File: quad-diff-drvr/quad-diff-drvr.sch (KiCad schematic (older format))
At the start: 10 parts, among them J1 Raspberry_Pi_2_3, J2 Conn_01x04, J3 Conn_01x04, J4 Conn_01x04, J5 Conn_01x04, J6 Conn_01x04

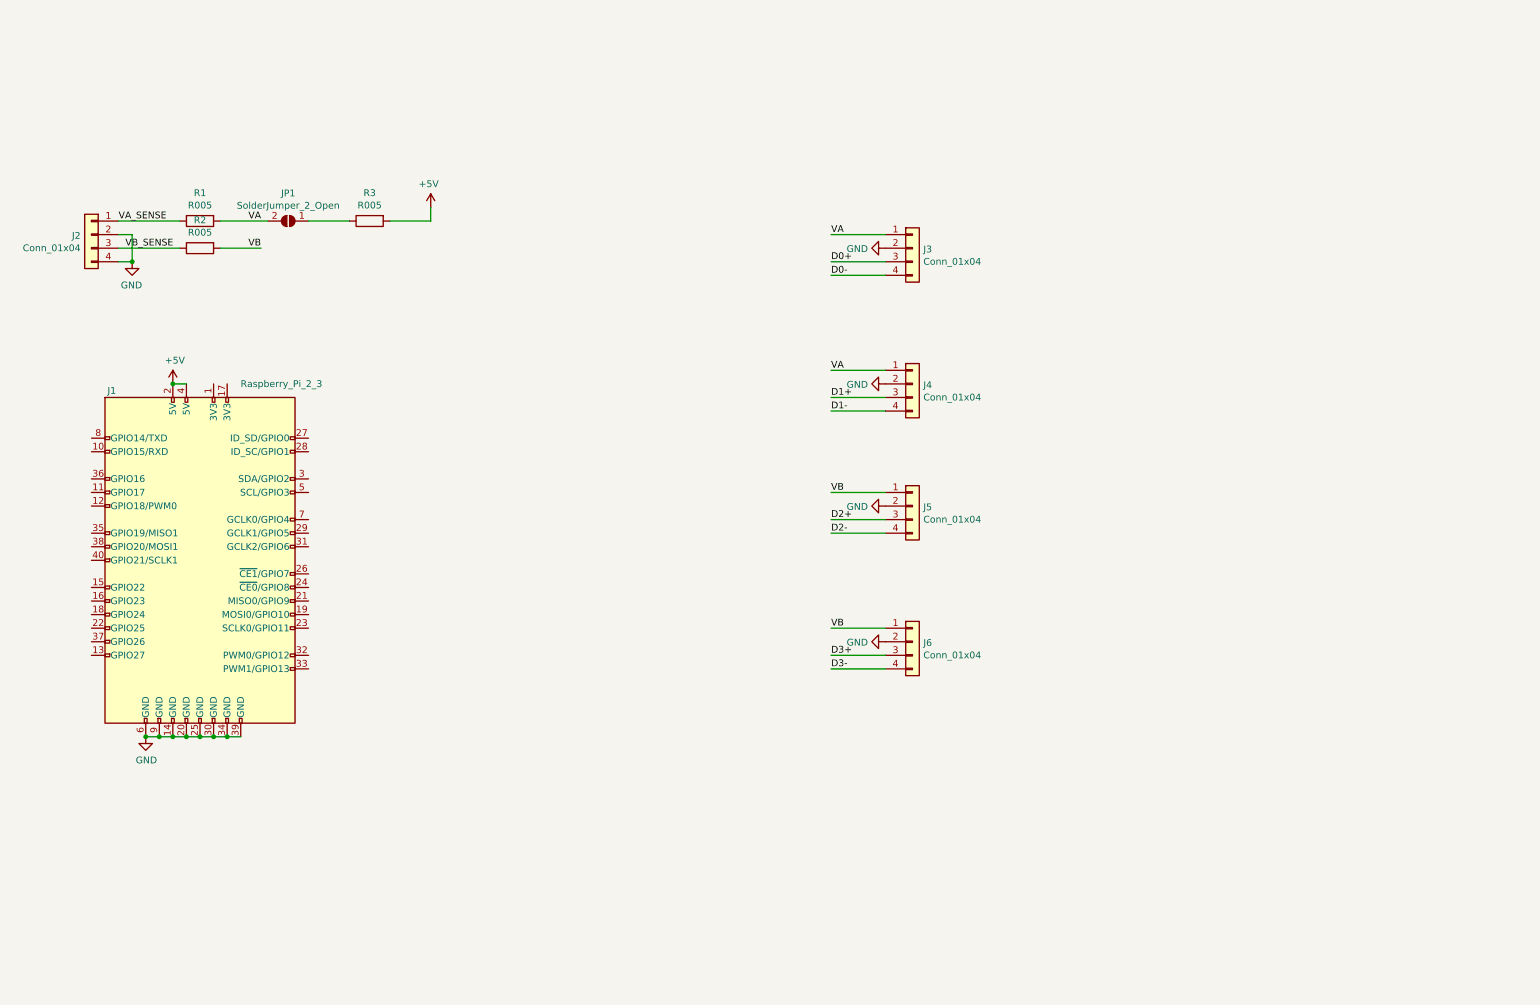
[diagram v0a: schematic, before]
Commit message: qdd: power monitor added
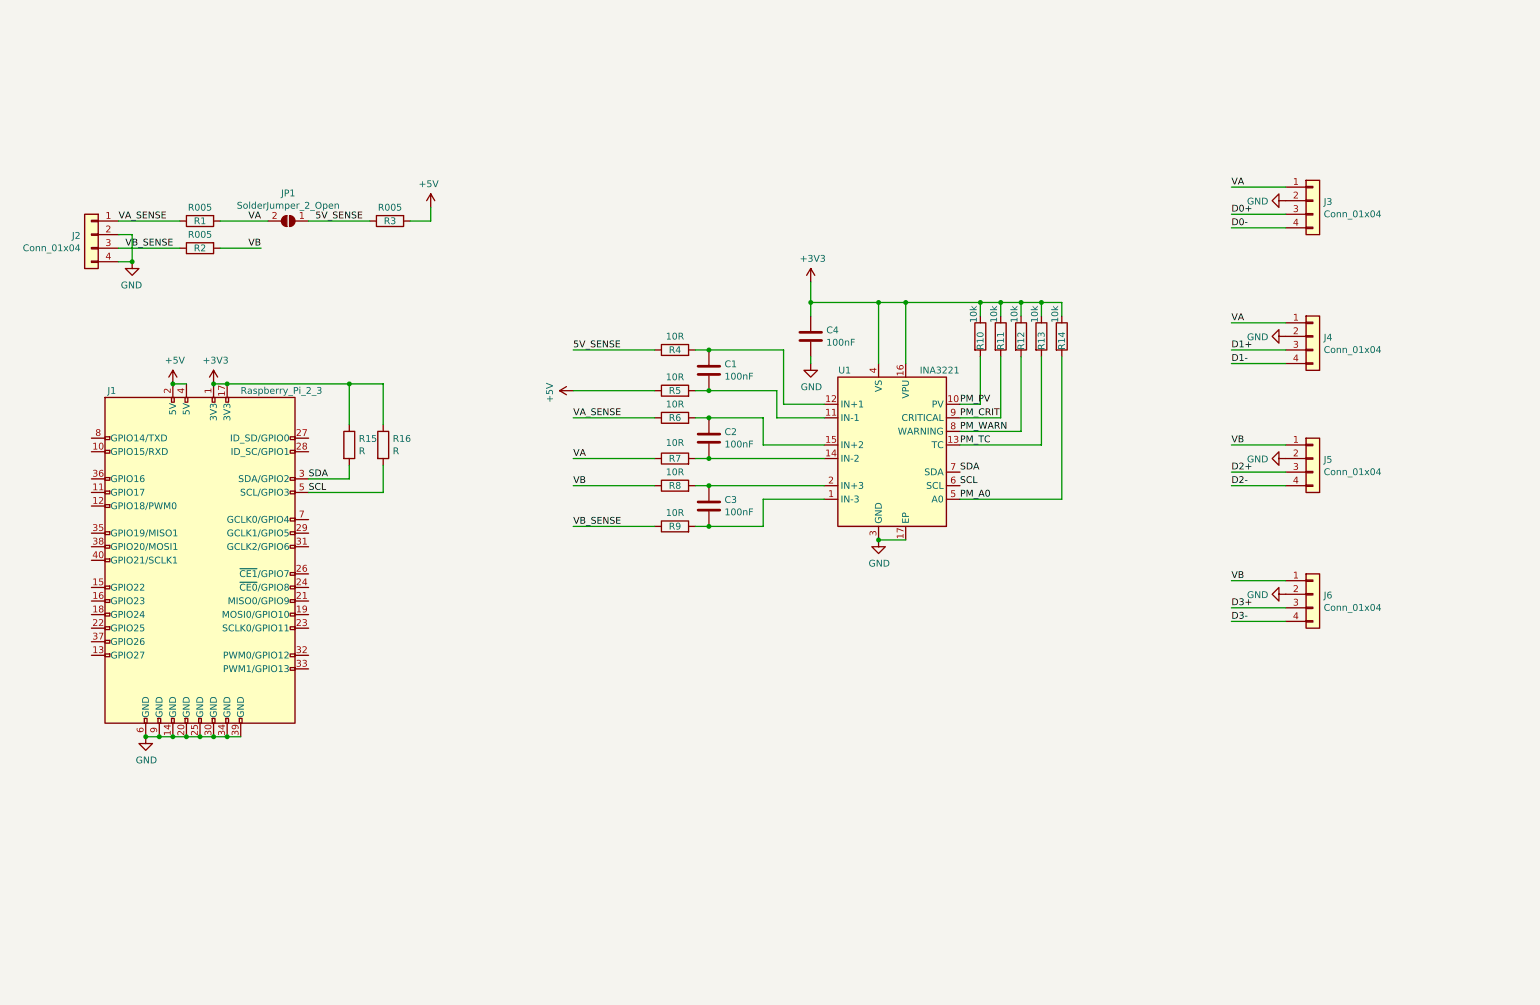
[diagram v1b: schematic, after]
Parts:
- added C1, C2, C3, C4: 100nF, Capacitor_SMD:C_0603_1608Metric, symbol Device:C
- added R10, R11, R12, R13, R14: 10k, Resistor_SMD:R_0603_1608Metric, symbol Device:R
- added R15, R16: R, Resistor_SMD:R_0603_1608Metric, symbol Device:R
- added R4, R5, R6, R7, R8, R9: 10R, Resistor_SMD:R_0603_1608Metric, symbol Device:R
- added U1: INA3221, Package_DFN_QFN:Texas_RGV_S-PVQFN-N16_EP2.1x2.1mm, symbol Power_Management:INA3221
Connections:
- net +5V: now also R5.1
- net GND: now also C4.2, U1.17 (EP), U1.3 (GND)
- net VA: now also R7.1
- net VA_SENSE: now also R6.1
- net VB: now also R8.1
- net VB_SENSE: now also R9.1
- net +3V3: now reaches J1.1 (3V3)
- net +3V3: now also J1.17 (3V3), C4.1, R10.1, R11.1, R12.1, R13.1, R14.1, R15.1, R16.1, U1.16 (VPU), U1.4 (VS)
- net SDA: now reaches J1.3 (SDA/GPIO2)
- net SDA: now also R15.2, U1.7 (SDA)
- net SCL: now reaches J1.5 (SCL/GPIO3)
- net SCL: now also R16.2, U1.6 (SCL)
- net 5V_SENSE: now reaches JP1.1 (A), R3.1
- net 5V_SENSE: now also R4.1
- new net: C3.2, R9.2, U1.1 (IN-3)
- new net: C1.2, R5.2, U1.11 (IN-1)
- new net: C1.1, R4.2, U1.12 (IN+1)
- new net: C2.2, R7.2, U1.14 (IN-2)
- new net: C2.1, R6.2, U1.15 (IN+2)
- new net: C3.1, R8.2, U1.2 (IN+3)
- new net PM_A0: R14.2, U1.5 (A0)
- new net PM_CRIT: R11.2, U1.9 (CRITICAL)
- new net PM_PV: R10.2, U1.10 (PV)
- new net PM_TC: R13.2, U1.13 (TC)
- new net PM_WARN: R12.2, U1.8 (WARNING)
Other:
- moved on the sheet: J3, J4, J5, J6, R3

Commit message: qdd: add mux0 and mux1
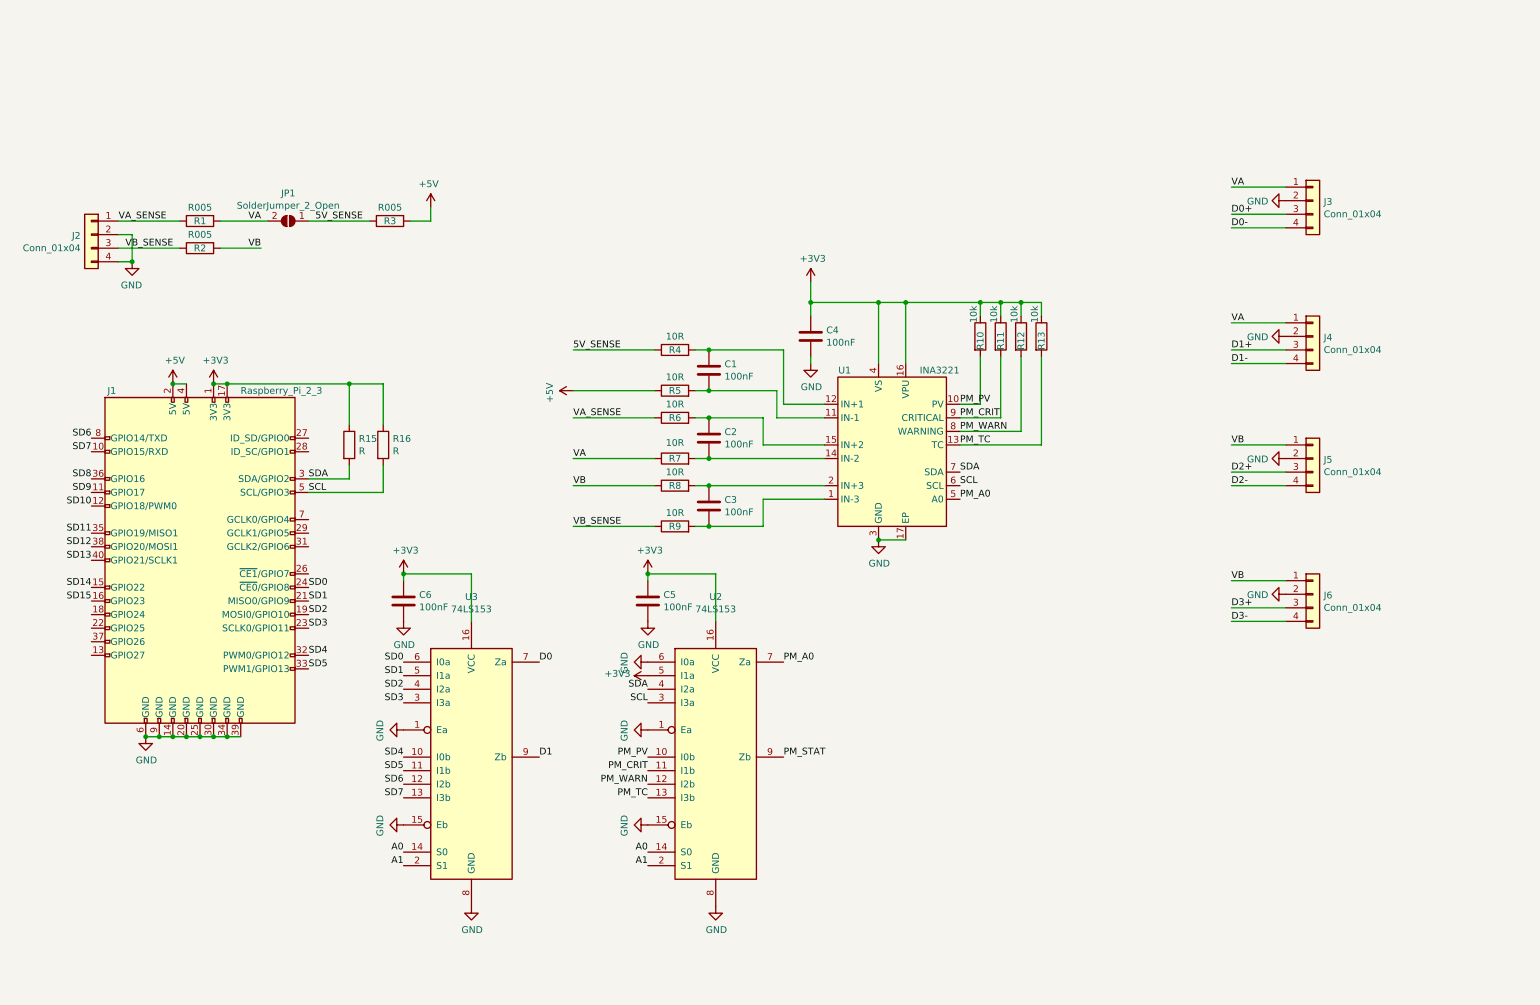
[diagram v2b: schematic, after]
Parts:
- removed R14: 10k, Resistor_SMD:R_0603_1608Metric, symbol Device:R
- added C5, C6: 100nF, Capacitor_SMD:C_0603_1608Metric, symbol Device:C
- added U2, U3: 74LS153, Package_SO:TSSOP-16_4.4x5mm_P0.65mm, symbol 74xx:74LS153
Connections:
- net +3V3: now also C5.1, C6.1, U2.16 (VCC), U2.5 (I1a), U3.16 (VCC)
- net GND: now also C5.2, C6.2, U2.1 (Ea), U2.15 (Eb), U2.6 (I0a), U2.8 (GND), U3.1 (Ea), U3.15 (Eb), U3.8 (GND)
- net PM_A0: now also U2.7 (Za)
- net PM_CRIT: now also U2.11 (I1b)
- net PM_PV: now also U2.10 (I0b)
- net PM_TC: now also U2.13 (I3b)
- net PM_WARN: now also U2.12 (I2b)
- net SCL: now also U2.3 (I3a)
- net SDA: now also U2.4 (I2a)
- net SD7: now reaches J1.10 (GPIO15/RXD)
- net SD7: now also U3.13 (I3b)
- net SD9: now reaches J1.11 (GPIO17)
- net SD10: now reaches J1.12 (GPIO18/PWM0)
- net SD14: now reaches J1.15 (GPIO22)
- net SD15: now reaches J1.16 (GPIO23)
- net SD2: now reaches J1.19 (MOSI0/GPIO10)
- net SD2: now also U3.4 (I2a)
- net SD1: now reaches J1.21 (MISO0/GPIO9)
- net SD1: now also U3.5 (I1a)
- net SD3: now reaches J1.23 (SCLK0/GPIO11)
- net SD3: now also U3.3 (I3a)
- net SD0: now reaches J1.24 (~CE0~/GPIO8)
- net SD0: now also U3.6 (I0a)
- net SD4: now reaches J1.32 (PWM0/GPIO12)
- net SD4: now also U3.10 (I0b)
- net SD5: now reaches J1.33 (PWM1/GPIO13)
- net SD5: now also U3.11 (I1b)
- net SD11: now reaches J1.35 (GPIO19/MISO1)
- net SD8: now reaches J1.36 (GPIO16)
- net SD12: now reaches J1.38 (GPIO20/MOSI1)
- net SD13: now reaches J1.40 (GPIO21/SCLK1)
- net SD6: now reaches J1.8 (GPIO14/TXD)
- net SD6: now also U3.12 (I2b)
- new net A0: U2.14 (S0), U3.14 (S0)
- new net A1: U2.2 (S1), U3.2 (S1)
- new net D0: U3.7 (Za)
- new net D1: U3.9 (Zb)
- new net PM_STAT: U2.9 (Zb)

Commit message: qd: GPIO expander in
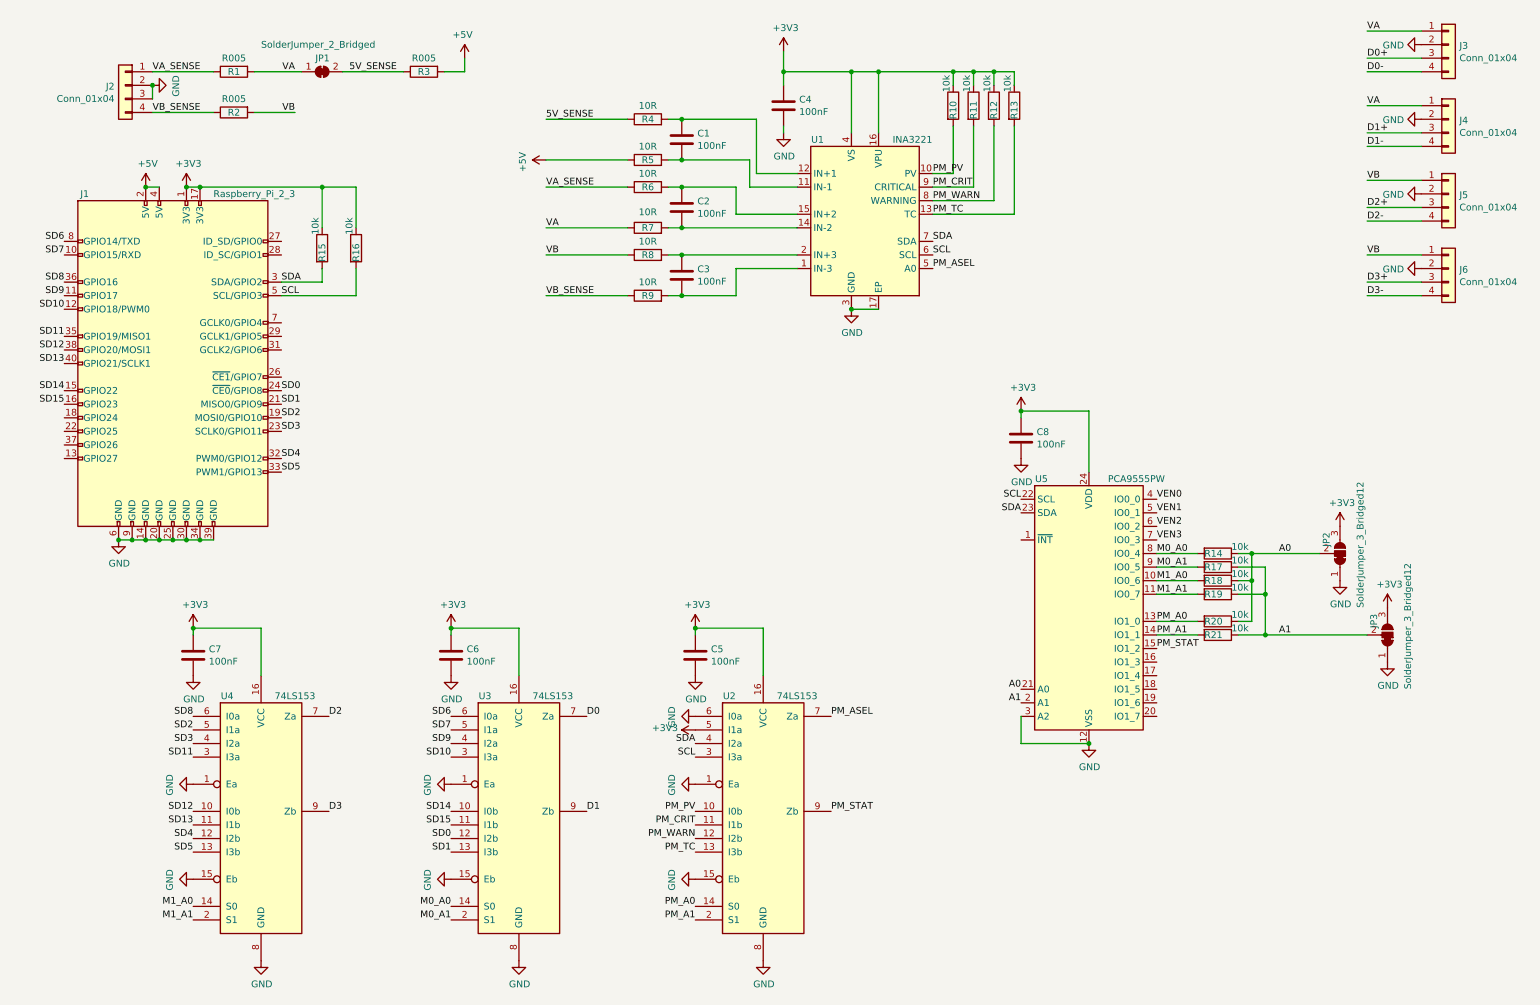
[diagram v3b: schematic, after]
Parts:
- removed JP1: SolderJumper_2_Open, Jumper:SolderJumper-2_P1.3mm_Open_RoundedPad1.0x1.5mm, symbol Jumper:SolderJumper_2_Open
- added C7, C8: 100nF, Capacitor_SMD:C_0603_1608Metric, symbol Device:C
- added JP1: SolderJumper_2_Bridged, Jumper:SolderJumper-2_P1.3mm_Bridged2Bar_RoundedPad1.0x1.5mm, symbol Jumper:SolderJumper_2_Bridged
- added JP2, JP3: SolderJumper_3_Bridged12, Jumper:SolderJumper-3_P1.3mm_Bridged2Bar12_RoundedPad1.0x1.5mm, symbol Jumper:SolderJumper_3_Bridged12
- added R14, R17, R18, R19, R20, R21: 10k, Resistor_SMD:R_0603_1608Metric, symbol Device:R
- added U4: 74LS153, Package_SO:TSSOP-16_4.4x5mm_P0.65mm, symbol 74xx:74LS153
- added U5: PCA9555PW, Package_SO:TSSOP-24_4.4x7.8mm_P0.65mm, symbol Interface_Expansion:PCA9555PW
- R15, R16: value R -> 10k
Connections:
- net +3V3: now also C7.1, C8.1, JP2.3 (B), JP3.3 (B), U4.16 (VCC), U5.24 (VDD)
- net 5V_SENSE: now also JP1.2 (B)
- net A0: now also JP2.2 (C), R14.1, R18.1, R20.1, U5.21 (A0); no longer U2.14 (S0), U3.14 (S0)
- net A1: now also JP3.2 (C), R17.1, R19.1, R21.1, U5.2 (A1); no longer U2.2 (S1), U3.2 (S1)
- net GND: now also J2.3 (Pin_3), C7.2, C8.2, JP2.1 (A), JP3.1 (A), U4.1 (Ea), U4.15 (Eb), U4.8 (GND), U5.12 (VSS), U5.3 (A2); no longer J2.4 (Pin_4)
- net PM_A0: now also U2.14 (S0), R20.2, U5.13 (IO1_0); no longer U1.5 (A0), U2.7 (Za)
- net PM_STAT: now also U5.15 (IO1_2)
- net SCL: now also U5.22 (SCL)
- net SD0: now also U3.12 (I2b); no longer U3.6 (I0a)
- net SD1: now also U3.13 (I3b); no longer U3.5 (I1a)
- net SD10: now also U3.3 (I3a)
- net SD11: now also U4.3 (I3a)
- net SD12: now also U4.10 (I0b)
- net SD13: now also U4.11 (I1b)
- net SD14: now also U3.10 (I0b)
- net SD15: now also U3.11 (I1b)
- net SD2: now also U4.5 (I1a); no longer U3.4 (I2a)
- net SD3: now also U4.4 (I2a); no longer U3.3 (I3a)
- net SD4: now also U4.12 (I2b); no longer U3.10 (I0b)
- net SD5: now also U4.13 (I3b); no longer U3.11 (I1b)
- net SD6: now also U3.6 (I0a); no longer U3.12 (I2b)
- net SD7: now also U3.5 (I1a); no longer U3.13 (I3b)
- net SD8: now also U4.6 (I0a)
- net SD9: now also U3.4 (I2a)
- net SDA: now also U5.23 (SDA)
- net VA: now also JP1.1 (A)
- net VB_SENSE: now also J2.4 (Pin_4); no longer J2.3 (Pin_3)
- new net D2: U4.7 (Za)
- new net D3: U4.9 (Zb)
- new net M0_A0: R14.2, U3.14 (S0), U5.8 (IO0_4)
- new net M0_A1: R17.2, U3.2 (S1), U5.9 (IO0_5)
- new net M1_A0: R18.2, U4.14 (S0), U5.10 (IO0_6)
- new net M1_A1: R19.2, U4.2 (S1), U5.11 (IO0_7)
- new net PM_A1: R21.2, U2.2 (S1), U5.14 (IO1_1)
- new net PM_ASEL: U1.5 (A0), U2.7 (Za)
- new net VEN0: U5.4 (IO0_0)
- new net VEN1: U5.5 (IO0_1)
- new net VEN2: U5.6 (IO0_2)
- new net VEN3: U5.7 (IO0_3)
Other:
- moved on the sheet: C1, C2, C3, C4, C5, C6, J1, J2, J3, J4, J5, J6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
